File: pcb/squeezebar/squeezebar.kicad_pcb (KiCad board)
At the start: 2 copper layers, 119.4 x 20.3 mm, 37 parts

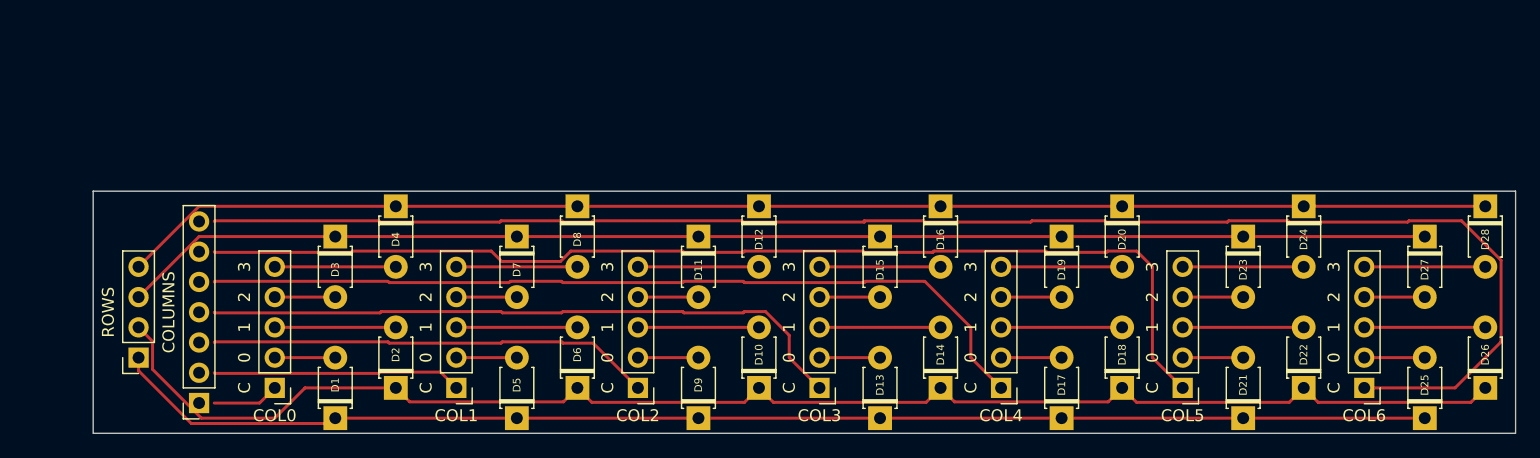
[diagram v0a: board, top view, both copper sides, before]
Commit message: Add mounting holes & extra side connectors
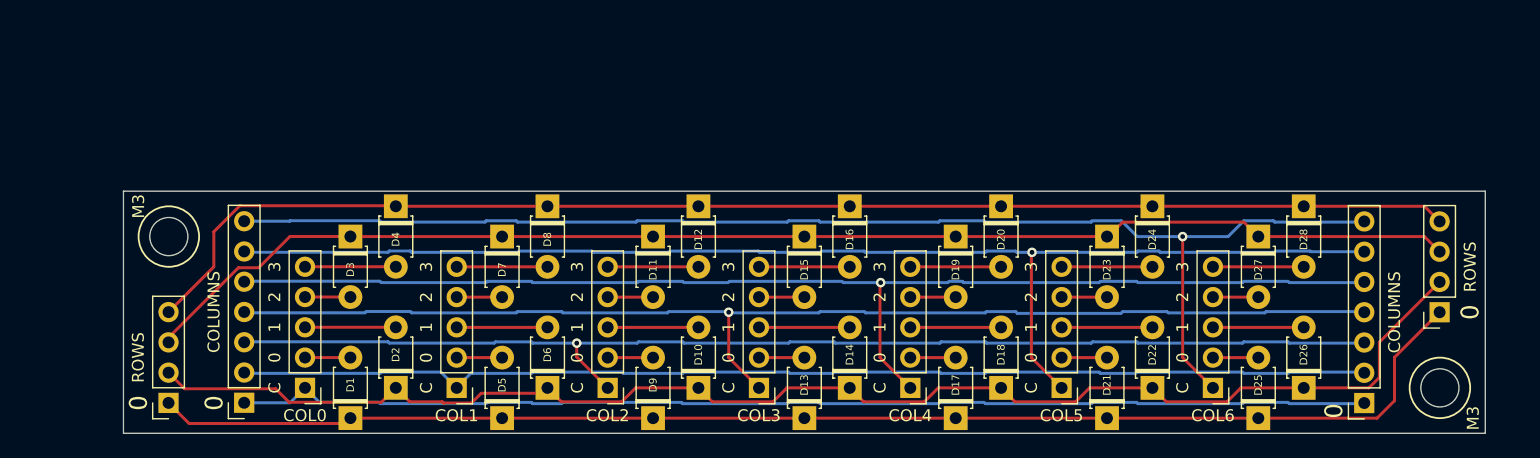
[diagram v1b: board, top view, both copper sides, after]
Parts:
- added COLUMNS: COLUMNS, Connector_PinSocket_2.54mm:PinSocket_1x07_P2.54mm_Vertical, F.Cu at (132.1, 90.2)
- added M3: ROWS, MountingHole:MountingHole_3.2mm_M3, F.Cu at (31.8, 76.2)
- added M3: MountingHole_3.2mm_M3, MountingHole:MountingHole_3.2mm_M3, F.Cu at (138.4, 88.9)
- added ROWS: ROWS, Connector_PinSocket_2.54mm:PinSocket_1x04_P2.54mm_Vertical, F.Cu at (138.4, 82.5)
- COL0, COL1, COL2, COL3, COL4, COL5, COL6: footprint Connector_PinHeader_2.54mm:PinHeader_1x05_P2.54mm_Vertical -> Library:PinHeader_1x05_P2.54mm_Vertical
- moved D26 15.2 mm to (127.0, 88.9)
- moved D28 15.2 mm to (127.0, 73.7)
- moved D25 14.0 mm to (123.2, 91.4)
- moved D27 14.0 mm to (123.2, 76.2)
- moved COL6 12.7 mm to (119.4, 88.9)
- moved D22 12.7 mm to (114.3, 88.9)
- moved D24 12.7 mm to (114.3, 73.7)
- moved D21 11.4 mm to (110.5, 91.4)
- moved D23 11.4 mm to (110.5, 76.2)
- moved D18 10.2 mm to (101.6, 88.9)
- moved D20 10.2 mm to (101.6, 73.7)
- moved COL5 10.2 mm to (106.7, 88.9)
- moved D17 8.89 mm to (97.8, 91.4)
- moved D19 8.89 mm to (97.8, 76.2)
- moved COL4 7.62 mm to (94.0, 88.9)
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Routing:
- net /c0: track 5.61 -> 95.6 mm
- net /c1: track 20.9 -> 95.7 mm
- net /c2: track 37.3 -> 99.3 mm, vias 0 -> 1
- net /c3: track 54.8 -> 101.9 mm, vias 0 -> 1
- net /c4: track 71.5 -> 104.4 mm, vias 0 -> 1
- net /c6: track 130.0 -> 109.4 mm, vias 0 -> 1
- net /c5: track 91.6 -> 107.0 mm, vias 0 -> 1
- net /r1: track 124.6 -> 118.9 mm
- net /r3: track 115.1 -> 112.6 mm
- net Net-(D20-Pad2): track 10.2 -> 7.62 mm
- net Net-(D18-Pad2): track 10.2 -> 7.62 mm
- net Net-(D24-Pad2): track 10.2 -> 7.62 mm
- net Net-(D22-Pad2): track 10.2 -> 7.62 mm
- net Net-(D8-Pad2): track 10.2 -> 7.62 mm
- net Net-(D6-Pad2): track 10.2 -> 7.62 mm
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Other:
- board size 119.4 x 20.3 mm -> 114.3 x 20.3 mm

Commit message: squeezebar: Switch to a more regular layout (WIP)
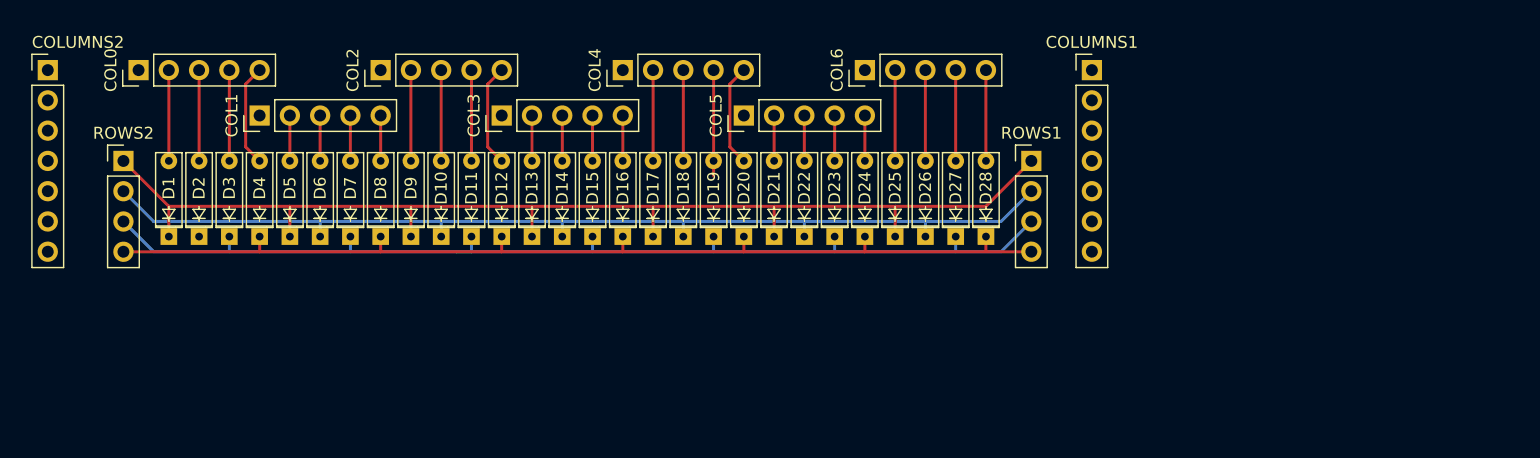
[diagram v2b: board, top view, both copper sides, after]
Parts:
- removed COLUMNS (x2): COLUMNS, Connector_PinSocket_2.54mm:PinSocket_1x07_P2.54mm_Vertical
- removed M3: ROWS, MountingHole:MountingHole_3.2mm_M3
- removed M3: MountingHole_3.2mm_M3, MountingHole:MountingHole_3.2mm_M3
- removed ROWS (x2): ROWS, Connector_PinSocket_2.54mm:PinSocket_1x04_P2.54mm_Vertical
- added COLUMNS1: COLUMNS1, Connector_PinHeader_2.54mm:PinHeader_1x07_P2.54mm_Vertical, F.Cu at (109.2, 62.2)
- added COLUMNS2: COLUMNS2, Connector_PinHeader_2.54mm:PinHeader_1x07_P2.54mm_Vertical, F.Cu at (21.6, 62.2)
- added ROWS1: ROWS1, Connector_PinHeader_2.54mm:PinHeader_1x04_P2.54mm_Vertical, F.Cu at (104.1, 69.8)
- added ROWS2: ROWS2, Connector_PinHeader_2.54mm:PinHeader_1x04_P2.54mm_Vertical, F.Cu at (27.9, 69.9)
- D1, D10, D11, D12, D13, D14, D15, D16, D17, D18, D19, D2, D20, D21, D22, D23, D24, D25, D26, D27, D28, D3, D4, D5, D6, D7, D8, D9: footprint Library:D_T-1_P5.08mm_Horizontal -> Library:Diode
- moved COL6 39.6 mm to (90.2, 62.2), turned to 90 degrees
- moved COL4 36.0 mm to (69.8, 62.2), turned to 90 degrees
- moved COL5 35.1 mm to (80.0, 66.0), turned to 90 degrees
- moved D26 34.2 mm to (95.2, 76.2), turned to 180 degrees
- moved D25 34.1 mm to (92.7, 76.2), turned to 180 degrees
- moved COL2 32.8 mm to (49.5, 62.2), turned to 90 degrees
- moved D22 31.9 mm to (85.1, 76.2), turned to 180 degrees
- moved D21 31.8 mm to (82.5, 76.2), turned to 180 degrees
- moved COL3 31.4 mm to (59.7, 66.0), turned to 90 degrees
- moved COL0 30.1 mm to (29.2, 62.2), turned to 90 degrees
- moved D17 29.6 mm to (72.4, 76.2), turned to 180 degrees
- moved D18 29.5 mm to (74.9, 76.2), turned to 180 degrees
- moved COL1 28.2 mm to (39.4, 66.0), turned to 90 degrees
- moved D13 27.5 mm to (62.2, 76.2), turned to 180 degrees
- moved D14 27.3 mm to (64.8, 76.2), turned to 180 degrees
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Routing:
- net /c6: track 109.4 -> 0.00 mm, vias 1 -> 0
- net /c5: track 107.0 -> 0.00 mm, vias 1 -> 0
- net /c4: track 104.4 -> 0.00 mm, vias 1 -> 0
- net /c3: track 101.9 -> 0.00 mm, vias 1 -> 0
- net /c2: track 99.3 -> 0.00 mm, vias 1 -> 0
- net /c1: track 95.7 -> 0.00 mm
- net /c0: track 95.6 -> 0.00 mm
- net /r1: track 118.9 -> 85.9 mm
- net /r3: track 112.6 -> 85.1 mm
- net /r2: track 111.7 -> 88.5 mm
- net /r0: track 112.8 -> 97.1 mm
- net Net-(COL4-Pad4): track 3.81 -> 8.89 mm
- net Net-(COL3-Pad5): track 7.62 -> 3.81 mm
- net Net-(COL3-Pad3): track 7.62 -> 3.81 mm
- net Net-(COL1-Pad5): track 7.62 -> 3.81 mm
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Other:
- board outline removed
- board text removed: "0"
- board text removed: "1"
- board text removed: "2"
- board text removed: "3"
- board text removed: "C"

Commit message: Squeezebar: New layout
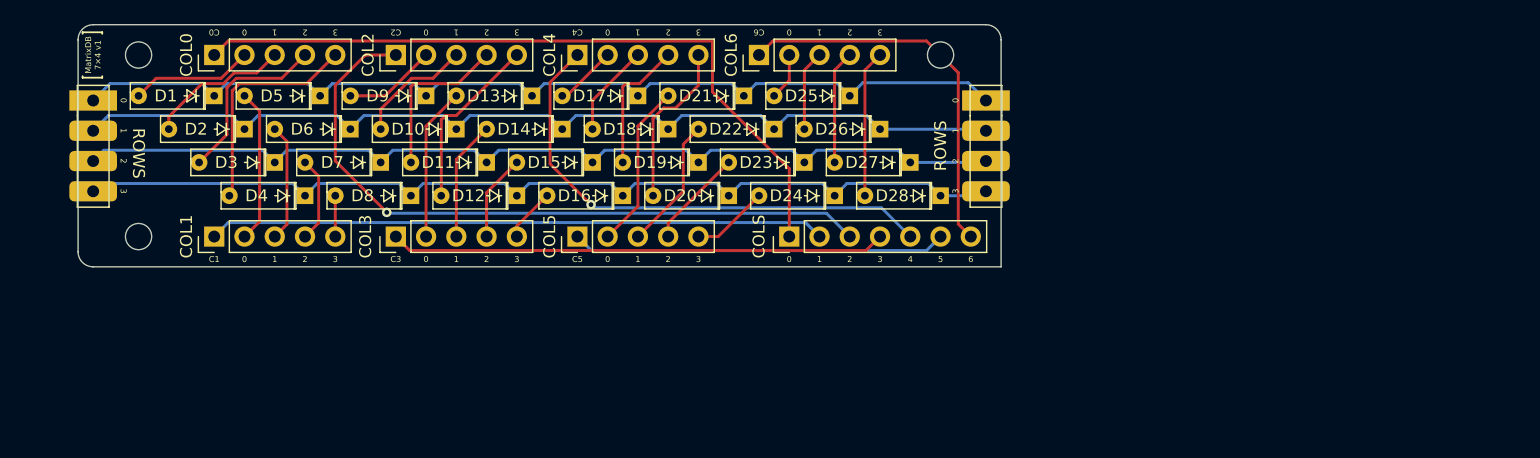
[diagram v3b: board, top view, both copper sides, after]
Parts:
- removed COLUMNS2: COLUMNS2, Connector_PinHeader_2.54mm:PinHeader_1x07_P2.54mm_Vertical
- added H1: MountingHole, MountingHole:MountingHole_2.2mm_M2_DIN965, F.Cu at (29.2, 76.2)
- added H2: MountingHole, MountingHole:MountingHole_2.2mm_M2_DIN965, F.Cu at (96.5, 61.0)
- added H3: MountingHole, MountingHole:MountingHole_2.2mm_M2_DIN965, F.Cu at (29.2, 61.0)
- COLUMNS1: value COLUMNS1 -> PINSOCKET
- ROWS1: value ROWS1 -> PINSOCKET; footprint Connector_PinHeader_2.54mm:PinHeader_1x04_P2.54mm_Vertical -> Library:PinSocket_1x04_P2.54mm_Vertical_LongPads
- ROWS2: value ROWS2 -> PINSOCKET; footprint Connector_PinHeader_2.54mm:PinHeader_1x04_P2.54mm_Vertical -> Library:PinSocket_1x04_P2.54mm_Vertical_LongPads
- moved COLUMNS1 29.0 mm to (83.8, 76.2), turned to 90 degrees
- moved COL5 17.3 mm to (66.0, 76.2)
- moved COL3 13.5 mm to (50.8, 76.2)
- moved D1 12.4 mm to (35.6, 64.4), turned to -90 degrees
- moved D25 12.4 mm to (88.9, 64.4), turned to -90 degrees
- moved D5 12.1 mm to (44.5, 64.4), turned to -90 degrees
- moved D21 12.1 mm to (80.0, 64.4), turned to -90 degrees
- moved D9 11.9 mm to (53.3, 64.4), turned to -90 degrees
- moved D17 11.9 mm to (71.1, 64.4), turned to -90 degrees
- moved D13 11.8 mm to (62.2, 64.4), turned to -90 degrees
- moved COL1 10.9 mm to (35.6, 76.2)
- moved D2 9.79 mm to (38.1, 67.2), turned to -90 degrees
- moved D26 9.79 mm to (91.4, 67.2), turned to -90 degrees
- moved D22 9.37 mm to (82.5, 67.2), turned to -90 degrees
- moved D6 9.37 mm to (47.0, 67.2), turned to -90 degrees
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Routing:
- net /c0: track 0.00 -> 61.4 mm
- net /c2: track 0.00 -> 58.3 mm, vias 0 -> 1
- net /c1: track 0.00 -> 51.8 mm
- net /c4: track 0.00 -> 42.5 mm, vias 0 -> 1
- net /c3: track 0.00 -> 41.6 mm
- net /c6: track 0.00 -> 32.5 mm
- net /c5: track 0.00 -> 31.5 mm
- net /r0: track 97.1 -> 82.1 mm
- net Net-(COL5-Pad2): track 3.81 -> 13.9 mm
- net Net-(COL0-Pad5): track 8.59 -> 18.6 mm
- net Net-(COL3-Pad2): track 3.81 -> 12.9 mm
- net Net-(COL1-Pad2): track 3.81 -> 12.9 mm
- net /r2: track 88.5 -> 80.9 mm
- net Net-(COL5-Pad3): track 3.81 -> 11.1 mm
- net Net-(COL0-Pad4): track 7.62 -> 14.9 mm
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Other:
- board outline added: 77.5 x 20.3 mm
- board text added: "0"
- board text added: "1"
- board text added: "2"
- board text added: "3"
- board text added: "4"
- board text added: "5"
- board text added: "6"
- board text added: "C0"
- board text added: "C1"
- board text added: "C2"
- board text added: "C3"
- board text added: "C4"
- board text added: "C5"
- board text added: "C6"
- board text added: "COLS"
- board text added: "MatrixDB 7×4 v1"
- board text added: "ROWS"

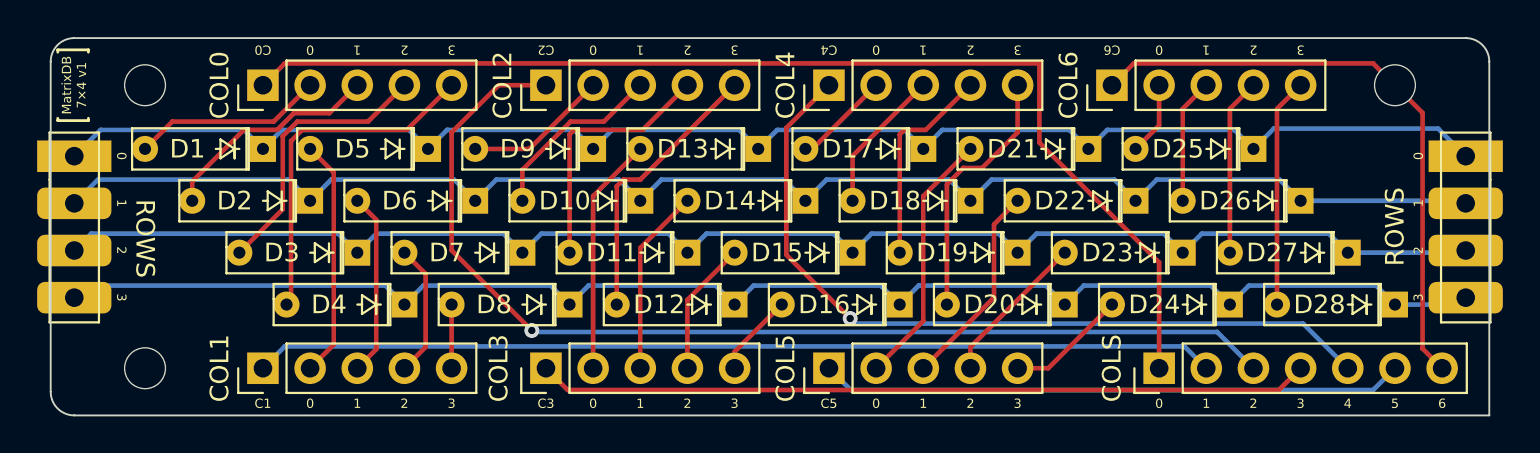
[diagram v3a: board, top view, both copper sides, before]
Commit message: Squeezebar (Matrix Daughterboard): Compact layout
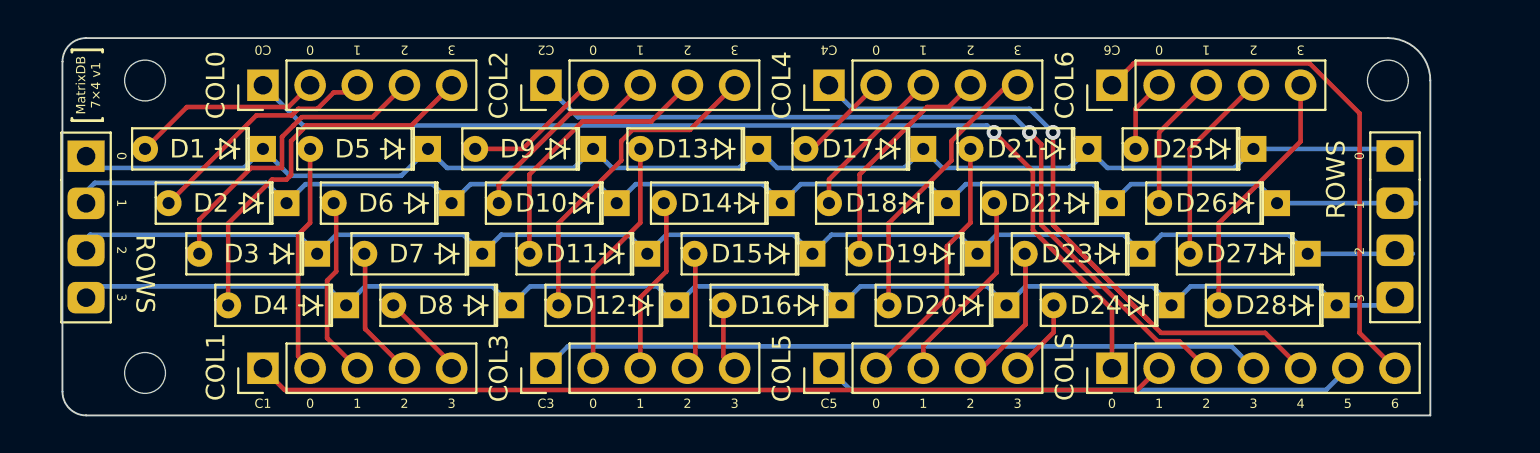
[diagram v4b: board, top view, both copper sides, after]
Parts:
- moved ROWS1 3.81 mm to (96.5, 64.8)
- moved D12 3.14 mm to (57.8, 72.8)
- moved D16 3.14 mm to (66.7, 72.8)
- moved D20 3.14 mm to (75.6, 72.8)
- moved D24 3.14 mm to (84.5, 72.8)
- moved D28 3.14 mm to (93.4, 72.8)
- moved D4 3.14 mm to (40.0, 72.8)
- moved D8 3.14 mm to (48.9, 72.8)
- moved COLUMNS1 2.54 mm to (81.3, 76.2)
- moved D11 2.16 mm to (56.3, 70.0)
- moved D15 2.16 mm to (65.1, 70.0)
- moved D19 2.16 mm to (74.0, 70.0)
- moved D23 2.16 mm to (82.9, 70.0)
- moved D27 2.16 mm to (91.8, 70.0)
- moved D3 2.16 mm to (38.5, 70.0)
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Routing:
- net /c2: track 58.3 -> 44.4 mm
- net /c0: track 61.4 -> 55.8 mm, vias 0 -> 1
- net /r0: track 82.1 -> 77.1 mm
- net /r3: track 80.9 -> 76.8 mm
- net /r1: track 81.7 -> 78.3 mm
- net /c6: track 32.5 -> 29.5 mm
- net /r2: track 80.9 -> 78.0 mm
- net Net-(COL2-Pad5): track 15.0 -> 17.6 mm
- net /c1: track 51.8 -> 49.2 mm
- net /c5: track 31.5 -> 28.9 mm
- net /c3: track 41.6 -> 39.1 mm
- net Net-(COL5-Pad5): track 6.50 -> 4.19 mm
- net Net-(COL0-Pad5): track 18.6 -> 20.6 mm
- net Net-(COL0-Pad4): track 14.9 -> 16.9 mm
- net Net-(COL3-Pad4): track 7.28 -> 5.70 mm
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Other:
- board size 77.5 x 20.3 mm -> 73.7 x 20.3 mm
- board text added: "COL0"
- board text added: "COL1"
- board text added: "COL2"
- board text added: "COL3"
- board text added: "COL4"
- board text added: "COL5"
- board text added: "COL6"
